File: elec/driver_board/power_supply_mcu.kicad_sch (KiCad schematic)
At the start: 3 parts

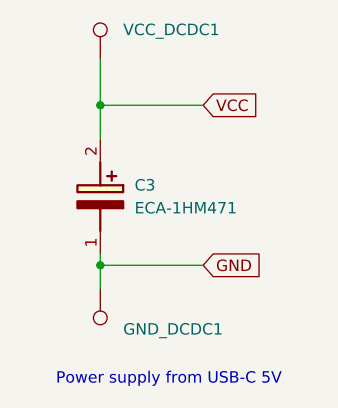
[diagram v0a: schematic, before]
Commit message: Update symbols
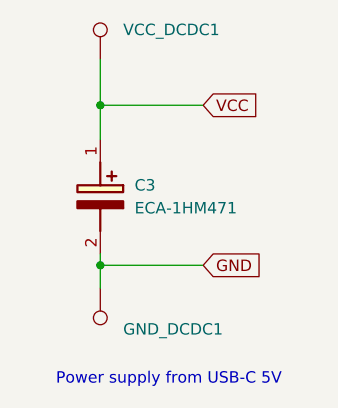
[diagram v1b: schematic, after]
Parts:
- C3: footprint Samacsys:CAPPRD500W65D1000H2200 -> Capacitor_THT:CP_Radial_D10.0mm_P5.00mm
- VCC_DCDC1: footprint TestPoint:TestPoint_Keystone_5000-5004_Miniature -> TestPoint:TestPoint_Keystone_5005-5009_Compact
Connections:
- net GND: now also C3.2 (-); no longer C3.1 (-)
- net VCC: now also C3.1 (+); no longer C3.2 (+)
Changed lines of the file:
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@@
 			)
 		)
-		(property "Footprint" "Samacsys:CAPPRD500W65D1000H2200"
+		(property "Footprint" "Capacitor_THT:CP_Radial_D10.0mm_P5.00mm"
 			(at 33.35 88.9 0)
 			(effects
@@
 			)
 		)
-		(property "Footprint" "TestPoint:TestPoint_Keystone_5000-5004_Miniature"
+		(property "Footprint" "TestPoint:TestPoint_Keystone_5005-5009_Compact"
 			(at 134.62 71.12 0)
 			(effects

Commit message: Update page number
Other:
- title: Power supply -> Clockclock
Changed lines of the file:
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@@
 	(paper "A4")
 	(title_block
-		(title "Power supply")
-		(date "2025-01-26")
-		(rev "2")
+		(title "Clockclock")
+		(date "2025-02-26")
+		(rev "3")
 	)
 	(text "Power supply from USB-C 5V"
